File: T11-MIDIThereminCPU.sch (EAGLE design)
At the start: 57 parts, among them IC1 UA78M05DCY, IC2 74AHC1G04DCK, IC3 74AHC1G04DCK, J1 DCJ0202, Q1 16MHz, U1 ATMEGA328P-AU

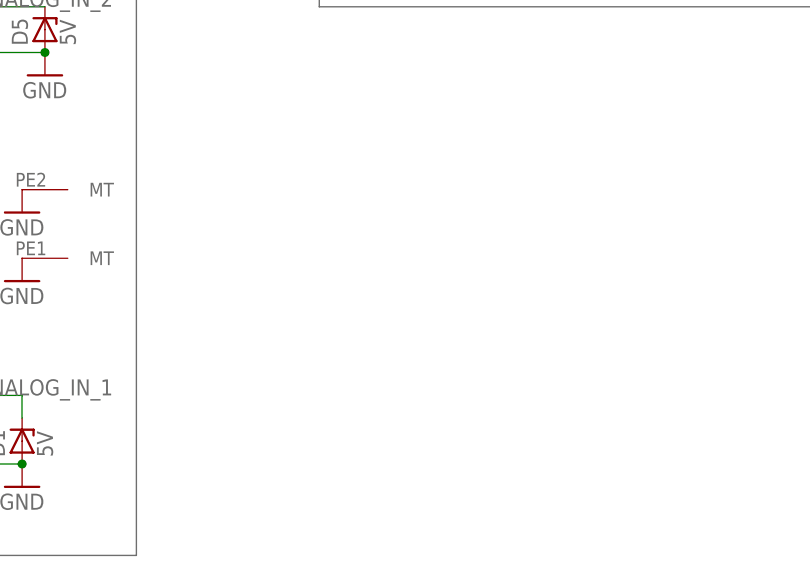
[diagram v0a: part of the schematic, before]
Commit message: Appended T11- to files.
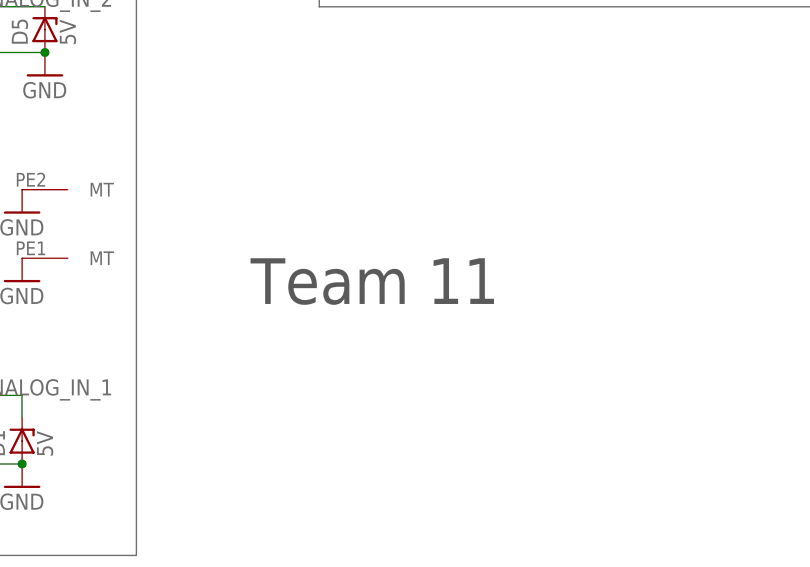
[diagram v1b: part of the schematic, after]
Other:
- note added: "Team 11"
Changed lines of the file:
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@@
 <wire x1="93.98" y1="134.62" x2="60.96" y2="134.62" width="0.1524" layer="95"/>
 <text x="66.04" y="137.16" size="1.778" layer="95" font="fixed">Test point header</text>
+<text x="182.88" y="27.94" size="5.08" layer="97">Team 11</text>
 </plain>
 <instances>

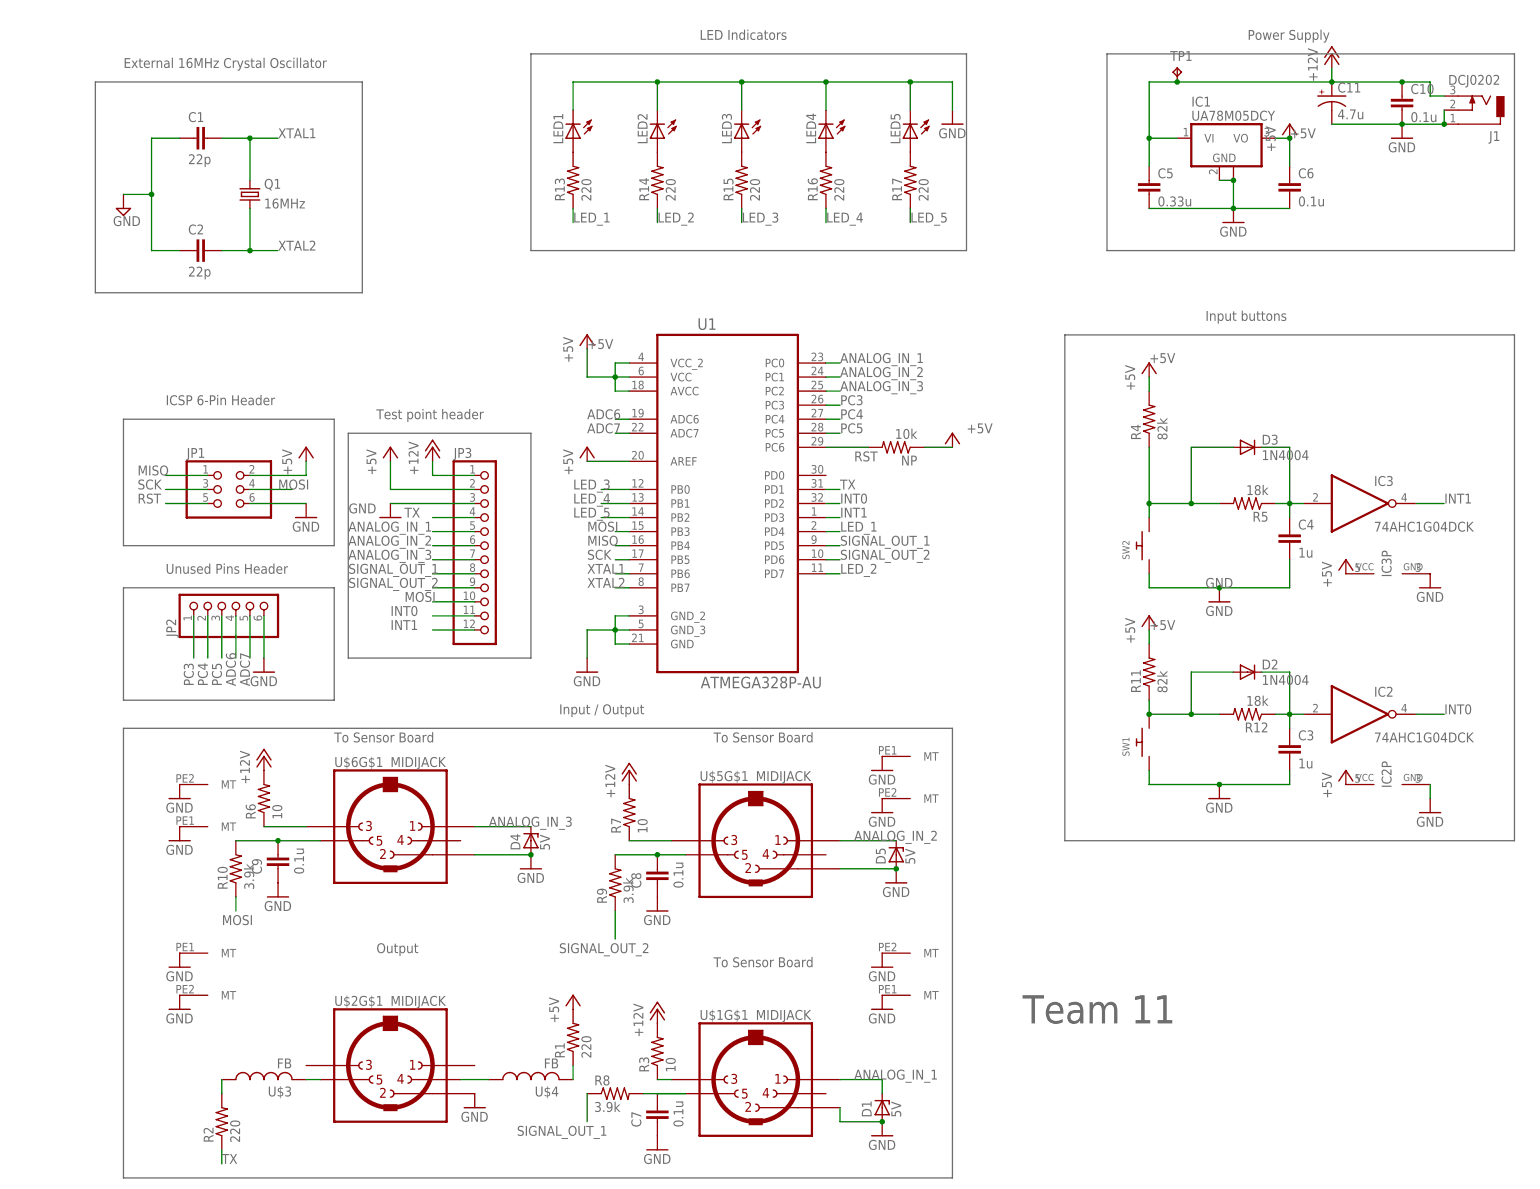
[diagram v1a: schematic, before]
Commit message: Added amplifiers
Added adjustable amplification onto the return signal from sensor
board. Named ICs. Some rearrangement.
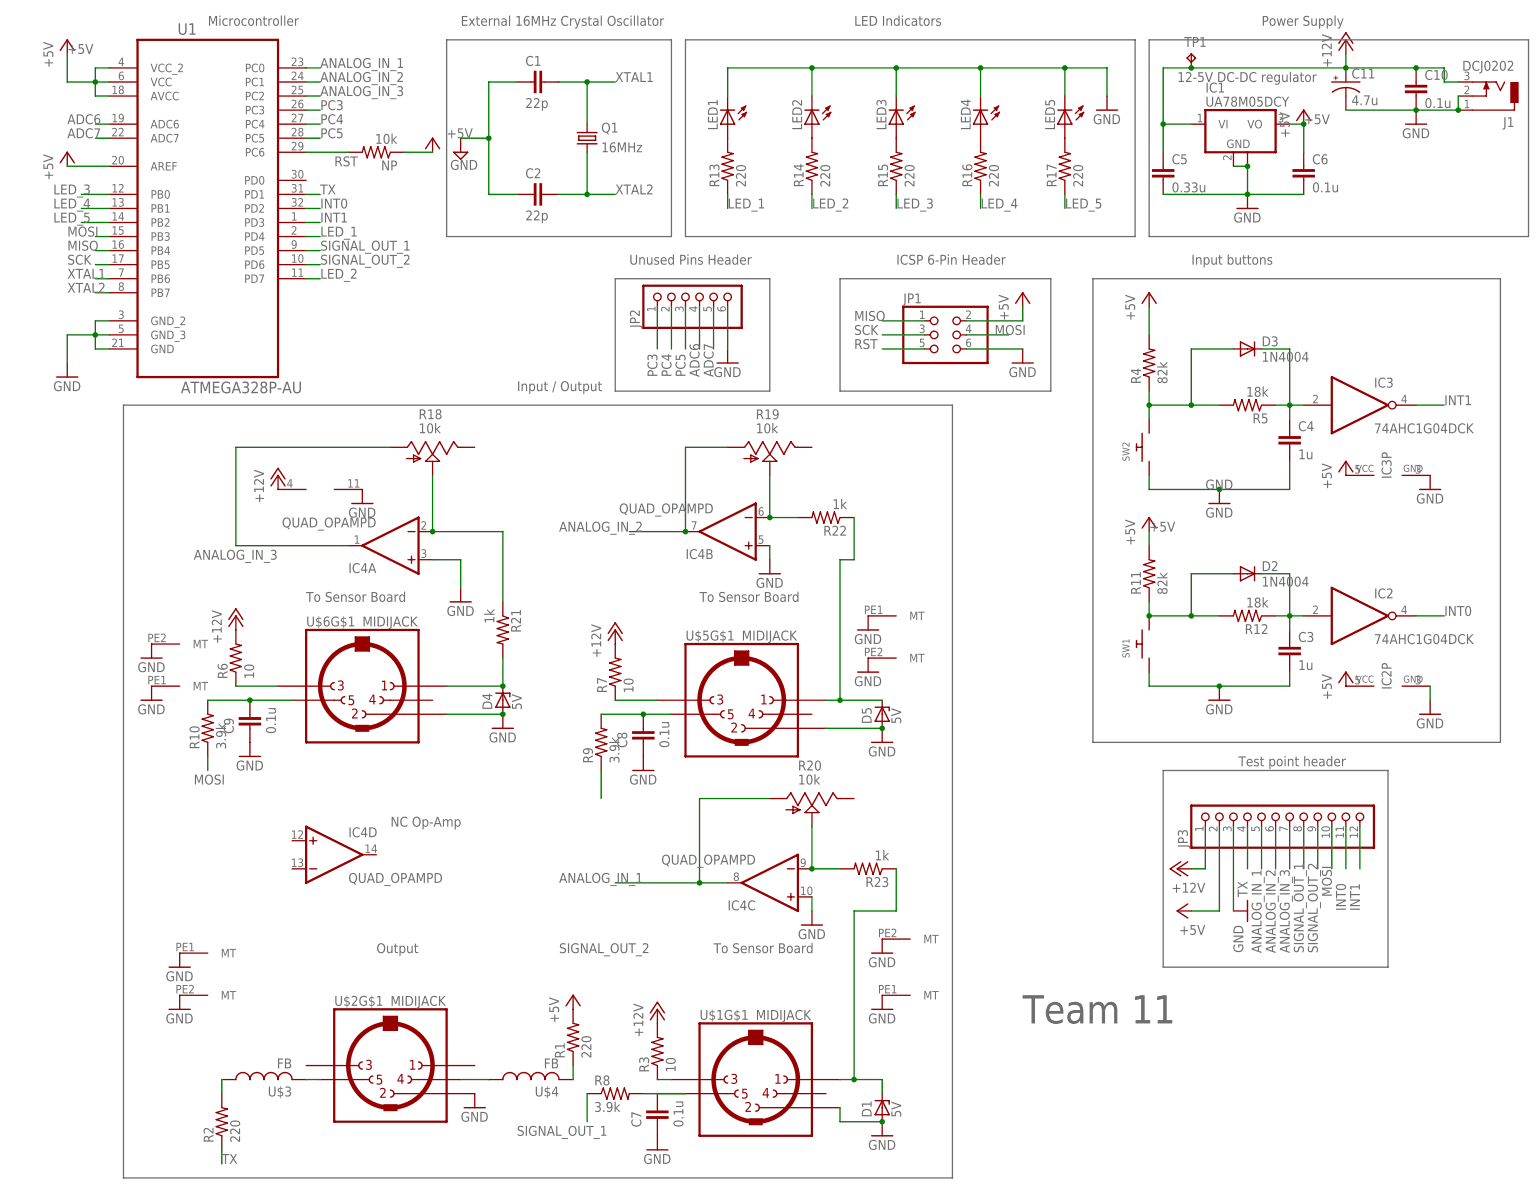
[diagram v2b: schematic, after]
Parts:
- added IC4: QUAD_OPAMPD, adafruit:QUAD_OPAMPD
- added R18, R19, R20: 10k, pot:TRIM_US-B25U
- added R21, R22, R23: 1k, resistor:R-US_0207/10
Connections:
- new net N$18: IC4C.-IN, R20.S, R23.2
- new net N$19: IC4A.-IN, R18.S, R21.1
- new net N$21: D1.C, R23.1, U$1G$1.1
- new net N$22: IC4B.-IN, R19.S, R22.2
- new net N$23: D4.C, R21.2, U$6G$1.1
- new net N$25: D5.C, R22.1, U$5G$1.1
- net +12V: now also IC4P.V+
- net ANALOG_IN_1: now also IC4C.OUT, R20.A; no longer D1.C, U$1G$1.1
- net ANALOG_IN_2: now also IC4B.OUT, R19.A; no longer D5.C, U$5G$1.1
- net ANALOG_IN_3: now also IC4A.OUT, R18.A; no longer D4.C, U$6G$1.1
- net GND: now also IC4A.+IN, IC4B.+IN, IC4C.+IN, IC4P.V-
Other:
- note added: "12-5V DC-DC regulator"
- note added: "Microcontroller"
- note added: "NC Op-Amp"
- moved on the sheet: C1, C10, C11, C2, C3, C4, C5, C6, C8, C9, D2, D3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

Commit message: Added ferrite bead values
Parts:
- U$3, U$4: value FB -> 1k@100MHz
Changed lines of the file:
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@@
 <part name="IC2" library="74xx-little-us" deviceset="74*1G04" device="DCK" technology="AHC"/>
 <part name="D2" library="diode" deviceset="1N4004" device=""/>
-<part name="U$3" library="adafruit" deviceset="FB" device=""/>
-<part name="U$4" library="adafruit" deviceset="FB" device=""/>
+<part name="U$3" library="adafruit" deviceset="FB" device="" value="1k@100MHz"/>
+<part name="U$4" library="adafruit" deviceset="FB" device="" value="1k@100MHz"/>
 <part name="IC3" library="74xx-little-us" deviceset="74*1G04" device="DCK" technology="AHC"/>
 <part name="R4" library="resistor" deviceset="R-US_" device="0207/10" value="82k"/>

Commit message: Changed filter values
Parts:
- C7, C8, C9: value 0.1u -> 100n
- R10, R8, R9: value 3.9k -> 1k
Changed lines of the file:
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@@
 <part name="D5" library="diode" deviceset="ZENER-DIODE" device="P1-Z12" value="5V"/>
 <part name="R7" library="resistor" deviceset="R-US_" device="0207/10" value="10"/>
-<part name="R8" library="resistor" deviceset="R-US_" device="0207/10" value="3.9k"/>
-<part name="C7" library="capacitor-wima" deviceset="C" device="2,5-3" value="0.1u"/>
-<part name="R9" library="resistor" deviceset="R-US_" device="0207/10" value="3.9k"/>
-<part name="C8" library="capacitor-wima" deviceset="C" device="2,5-3" value="0.1u"/>
-<part name="R10" library="resistor" deviceset="R-US_" device="0207/10" value="3.9k"/>
-<part name="C9" library="capacitor-wima" deviceset="C" device="2,5-3" value="0.1u"/>
+<part name="R8" library="resistor" deviceset="R-US_" device="0207/10" value="1k"/>
+<part name="C7" library="capacitor-wima" deviceset="C" device="2,5-3" value="100n"/>
+<part name="R9" library="resistor" deviceset="R-US_" device="0207/10" value="1k"/>
+<part name="C8" library="capacitor-wima" deviceset="C" device="2,5-3" value="100n"/>
+<part name="R10" library="resistor" deviceset="R-US_" device="0207/10" value="1k"/>
+<part name="C9" library="capacitor-wima" deviceset="C" device="2,5-3" value="100n"/>
 <part name="LED1" library="adafruit" deviceset="LED" device="B155"/>
 <part name="LED2" library="adafruit" deviceset="LED" device="B155"/>

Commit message: Initial
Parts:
- removed IC2, IC3: 74AHC1G04DCK, 74xx-little-us:74AHC1G04DCK
- removed TP1: TPTP15SQ, testpad:TPTP15SQ
- added IC5: 4069D, 40xx:4069D
- D1, D4, D5: device diode:ZENER-DIODEP1-Z12 -> diode:ZENER-DIODEDO35Z10
- LED1, LED2, LED3, LED4, LED5: device adafruit:LEDB155 -> adafruit:LED3MM
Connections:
- net +12V: no longer TP1.TP
- net +5V: now also IC5P.VDD; no longer IC2P.VCC, IC3P.VCC
- net GND: now also IC5P.VSS; no longer IC2P.GND, IC3P.GND
- net INT0: now also IC5B.O; no longer IC2A.O
- net INT1: now also IC5A.O; no longer IC3A.O
- net N$14: now also IC5B.I; no longer IC2A.I
- net N$6: now also IC5A.I; no longer IC3A.I
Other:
- note added: "NC Inverter pins"

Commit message: Board creation
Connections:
- net GND: now also IC4D.+IN, IC4D.-IN, IC5C.I, IC5D.I, IC5E.I, IC5F.I
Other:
- moved on the sheet: IC5D, IC5F
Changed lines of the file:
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@@
 <part name="P+5" library="supply1" deviceset="+5V" device=""/>
 <part name="GND5" library="supply1" deviceset="GND" device=""/>
+<part name="GND6" library="supply1" deviceset="GND" device=""/>
+<part name="GND31" library="supply1" deviceset="GND" device=""/>
+<part name="GND32" library="supply1" deviceset="GND" device=""/>
+<part name="GND33" library="supply1" deviceset="GND" device=""/>
+<part name="GND34" library="supply1" deviceset="GND" device=""/>
+<part name="GND35" library="supply1" deviceset="GND" device=""/>
 </parts>
 <sheets>
@@
 <instance part="IC5" gate="B" x="243.84" y="101.6"/>
 <instance part="IC5" gate="C" x="187.96" y="127" rot="R90"/>
-<instance part="IC5" gate="D" x="187.96" y="104.14" rot="R90"/>
+<instance part="IC5" gate="D" x="187.96" y="96.52" rot="R90"/>
 <instance part="IC5" gate="E" x="175.26" y="127" rot="R90"/>
-<instance part="IC5" gate="F" x="175.26" y="104.14" rot="R90"/>
+<instance part="IC5" gate="F" x="175.26" y="96.52" rot="R90"/>
 <instance part="IC5" gate="P" x="243.84" y="119.38" rot="R90"/>
 <instance part="P+5" gate="1" x="236.22" y="121.92"/>
 <instance part="GND5" gate="1" x="251.46" y="116.84"/>
+<instance part="GND6" gate="1" x="175.26" y="114.3"/>
+<instance part="GND31" gate="1" x="187.96" y="114.3"/>
+<instance part="GND32" gate="1" x="175.26" y="83.82"/>
+<instance part="GND33" gate="1" x="187.96" y="83.82"/>
+<instance part="GND34" gate="1" x="48.26" y="60.96" rot="R270"/>
+<instance part="GND35" gate="1" x="48.26" y="55.88" rot="R270"/>
 </instances>
 <busses>
@@
 <pinref part="GND5" gate="1" pin="GND"/>
 </segment>
+<segment>
+<pinref part="IC5" gate="E" pin="I"/>
+<pinref part="GND6" gate="1" pin="GND"/>
+</segment>
+<segment>
+<pinref part="IC5" gate="C" pin="I"/>
+<pinref part="GND31" gate="1" pin="GND"/>
+</segment>
+<segment>
+<pinref part="IC5" gate="F" pin="I"/>
+<pinref part="GND32" gate="1" pin="GND"/>
+</segment>
+<segment>
+<pinref part="IC5" gate="D" pin="I"/>
+<pinref part="GND33" gate="1" pin="GND"/>
+</segment>
+<segment>
+<pinref part="IC4" gate="D" pin="+IN"/>
+<pinref part="GND34" gate="1" pin="GND"/>
+</segment>
+<segment>
+<pinref part="IC4" gate="D" pin="-IN"/>
+<pinref part="GND35" gate="1" pin="GND"/>
+</segment>
 </net>
 <net name="MISO" class="0">
@@
 <pinref part="C7" gate="G$1" pin="2"/>
 <wire x1="116.84" y1="15.24" x2="121.92" y2="15.24" width="0.1524" layer="91"/>
-</segment>
-</net>
+<junction x="121.92" y="15.24"/>
+</segment>
+</net>
